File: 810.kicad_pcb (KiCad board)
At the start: 2 copper layers, 148 x 110 mm, 331 parts, among them J1 PJ301BM, J10 PJ301BM, J11 PJ301BM, J12 PJ301BM, J13 PJ301BM, J14 PJ301BM, J15 JACK_MONO_SW, J16 PJ301BM, J17 PJ301B, J18 PJ301B, J2 PJ301BM, J3 PJ301BM, J4 PJ301B, J5 PJ301B, J6 PJ301BM, J7 PJ301BM, J8 PJ301BM, J9 PJ301BM, P1 CONN_01X08, P2 CONN_02X05, P3 CONN_01X03, P4 CONN_01X08, P5 CONN_01X02, P6 CONN_02X03, Q1 PMBT2369, Q10 2SK208-GR, Q11 2SC4738, Q12 2SA1832, Q13 2SA1832, Q14 2SA1832, Q15 2SC4738, Q2 2SK208-GR, Q3 2SA1618, Q4 2SC4207, Q5 2SK208-GR, Q6 MMBF4391LT1G, Q7 2SA1832, Q8 PMBT2369, Q9 2SK208-GR, SW1 SPDT, SW2 SPDT, SW3 BF3-1050, SW4 SPDT, SW5 DP6T-ALPHA-SR2511, U1 TL072-, U10 TL072-, U11 TL072-, U12 TA75S558F, U13 TA75S558F, U14 TA75S558F, U15 TA75S558F, U16 TA75S558F, U17 CD4052, U18 TA75S558F, U19 TL072-, U2 TL072-, U20 CD4013, U3 TL072-, U4 CD40106, U5 CD4027, U6 LM13700, U7 LM13700, U8 LM13700, U9 TL072-

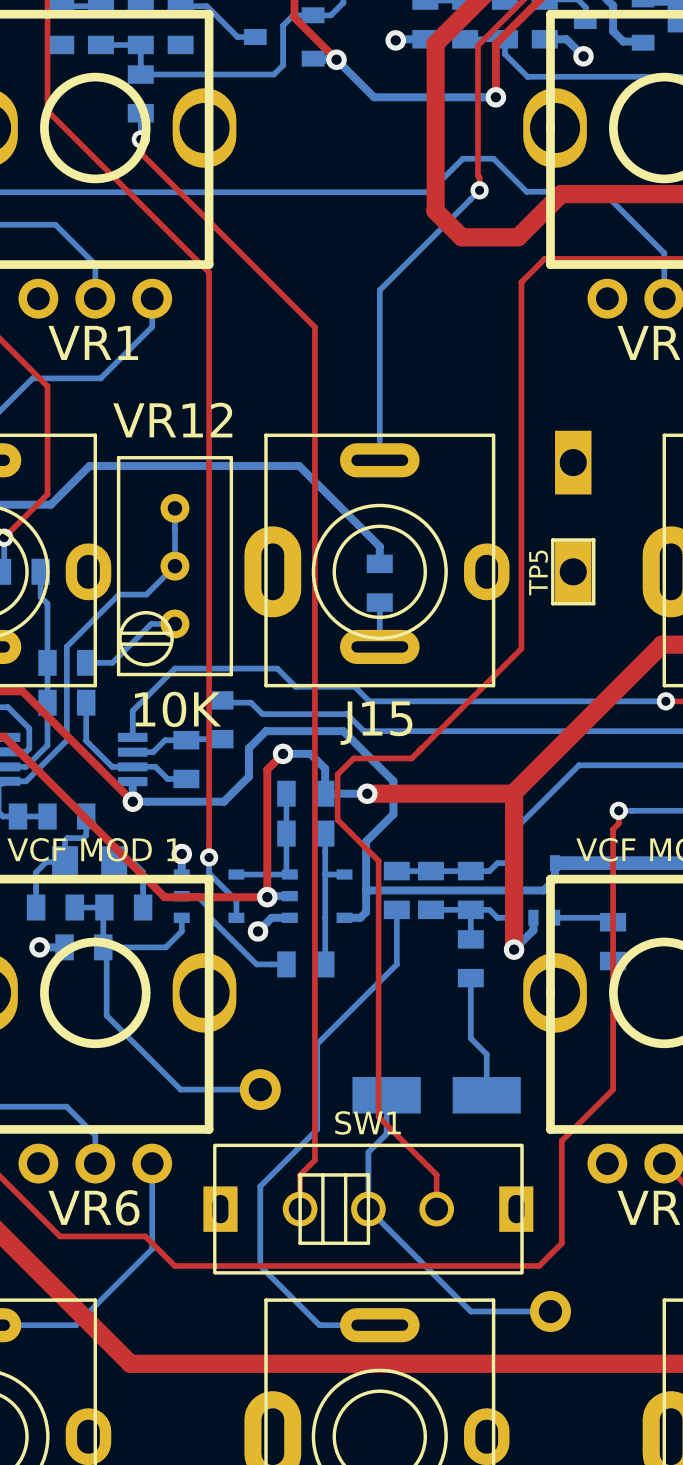
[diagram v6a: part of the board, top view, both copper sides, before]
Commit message: fixed position of middle switch, offset by 0.5 mm
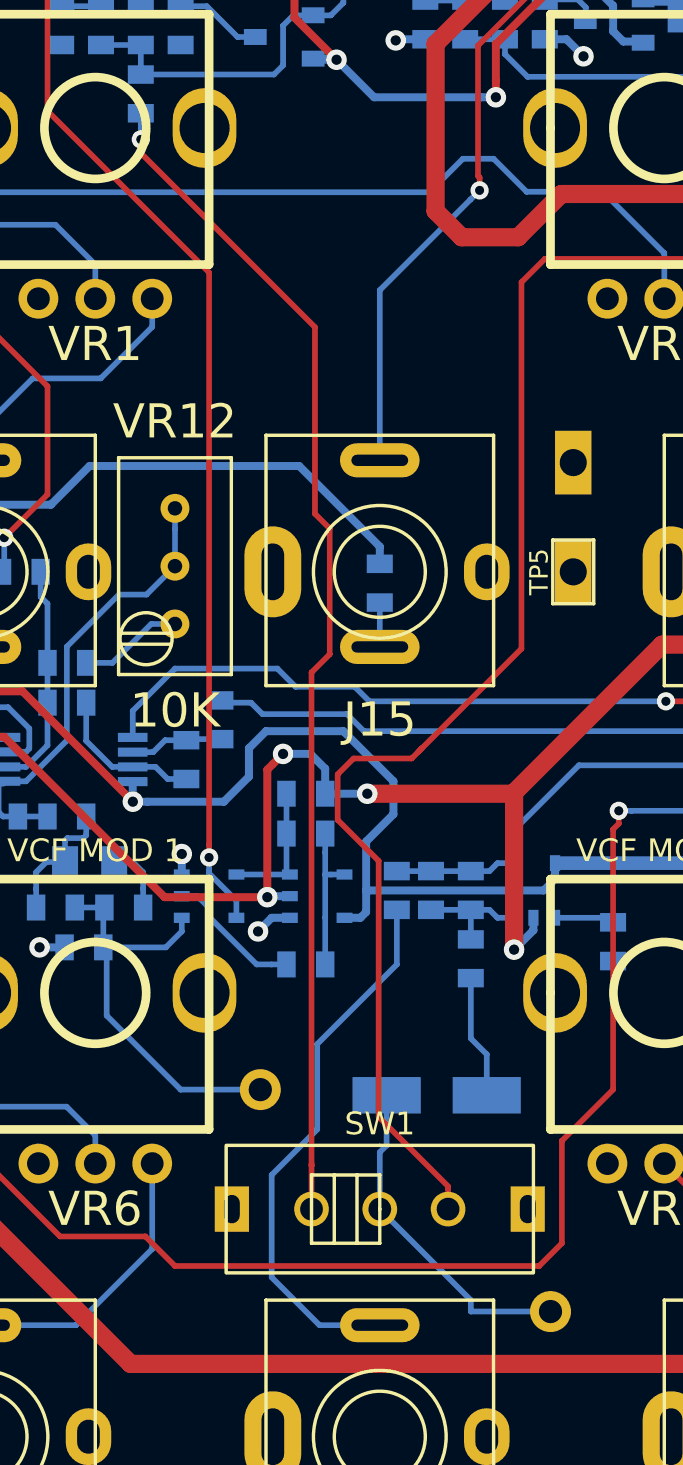
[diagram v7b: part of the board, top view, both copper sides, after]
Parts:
- moved SW1 0.50 mm to (158.0, 135.5)
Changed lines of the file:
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@@
     (area 78.467857 38.411038 232.878334 151.100001)
     (thickness 1.6)
-    (drawings 152)
-    (tracks 2178)
+    (drawings 148)
+    (tracks 2183)
     (zones 0)
     (modules 331)
@@
     (34 B.Paste user)
     (35 F.Paste user)
-    (36 B.SilkS user)
+    (36 B.SilkS user hide)
     (37 F.SilkS user)
     (38 B.Mask user)
@@
     (40 Dwgs.User user)
     (41 Cmts.User user)
-    (42 Eco1.User user hide)
+    (42 Eco1.User user)
     (43 Eco2.User user)
     (44 Edge.Cuts user)
@@
     (pad_to_paste_clearance -0.05)
     (aux_axis_origin 0 0)
-    (visible_elements 7FFFF7FF)
+    (visible_elements 7FFCF7FF)
     (pcbplotparams
-      (layerselection 0x010f0_80000001)
-      (usegerberextensions true)
-      (excludeedgelayer true)
+      (layerselection 0x01400_00000000)
+      (usegerberextensions false)
+      (excludeedgelayer false)
       (linewidth 0.200000)
       (plotframeref false)
@@
       (plotinvisibletext false)
       (padsonsilk false)
-      (subtractmaskfromsilk true)
-      (outputformat 1)
+      (subtractmaskfromsilk false)
+      (outputformat 3)
       (mirror false)
       (drillshape 0)
@@
   )
   (module MyModules:SS-12F108-1P2T-SLIDE (layer F.Cu)
-    (at 157.5 135.5)
+    (at 158 135.5)
     (descr http://www.taydaelectronics.com/datasheets/A-5111.pdf)
     (tags "1P2T, A-5111, TAYDA")
@@
   (gr_line (start 96.74 99.97) (end 94.46 99.97) (angle 90) (layer Eco1.User) (width 0.2))
   (gr_line (start 95.5 98.75) (end 95.5 101) (angle 90) (layer Eco1.User) (width 0.2))
-  (gr_line (start 209.5 132) (end 206.5 132) (angle 90) (layer Eco1.User) (width 0.2))
-  (gr_line (start 208 130.5) (end 208 133.75) (angle 90) (layer Eco1.User) (width 0.2))
-  (gr_line (start 159.5 132) (end 156.5 132) (angle 90) (layer Eco1.User) (width 0.2))
-  (gr_line (start 158 130.5) (end 158 133.5) (angle 90) (layer Eco1.User) (width 0.2))
-  (gr_line (start 109.5 132) (end 106.5 132) (angle 90) (layer Eco1.User) (width 0.2))
-  (gr_line (start 108 130.5) (end 108 133.5) (angle 90) (layer Eco1.User) (width 0.2))
+  (gr_line (start 209.5 135.5) (end 206.5 135.5) (angle 90) (layer Eco1.User) (width 0.2))
+  (gr_line (start 208 134) (end 208 137.25) (angle 90) (layer Eco1.User) (width 0.2))
+  (gr_line (start 159.5 135.5) (end 156.5 135.5) (angle 90) (layer Eco1.User) (width 0.2))
+  (gr_line (start 158 134) (end 158 137) (angle 90) (layer Eco1.User) (width 0.2))
+  (gr_line (start 109.5 135.5) (end 106.5 135.5) (angle 90) (layer Eco1.User) (width 0.2))
+  (gr_line (start 108 134) (end 108 137) (angle 90) (layer Eco1.User) (width 0.2))
   (gr_line (start 146.63 110.44) (end 148.88 110.44) (layer Eco1.User) (width 0.1))
   (gr_line (start 147.73 109.29) (end 147.73 111.6) (layer Eco1.User) (width 0.1))
@@
   (gr_line (start 158.001092 147.500117) (end 158.001092 143.500117) (layer Eco1.User) (width 0.1))
   (gr_line (start 156.00109 145.500117) (end 160.00109 145.500117) (layer Eco1.User) (width 0.1))
-  (gr_line (start 158.001092 139.428279) (end 158.001092 135.428279) (layer Eco1.User) (width 0.1))
-  (gr_line (start 156.00109 137.428279) (end 160.00109 137.428279) (layer Eco1.User) (width 0.1))
   (gr_line (start 175.501093 147.500117) (end 175.501093 143.500117) (layer Eco1.User) (width 0.1))
   (gr_line (start 173.501092 145.500117) (end 177.501092 145.500117) (layer Eco1.User) (width 0.1))
@@
   (gr_line (start 208.001099 147.500117) (end 208.001099 143.500117) (layer Eco1.User) (width 0.1))
   (gr_line (start 206.001097 145.500117) (end 210.001098 145.500117) (layer Eco1.User) (width 0.1))
-  (gr_line (start 208.001099 139.428279) (end 208.001099 135.428279) (layer Eco1.User) (width 0.1))
-  (gr_line (start 206.001097 137.428279) (end 210.001098 137.428279) (layer Eco1.User) (width 0.1))
   (gr_line (start 220.501088 128.004471) (end 220.501088 124.004471) (layer Eco1.User) (width 0.1))
   (gr_line (start 218.501086 126.004471) (end 222.501087 126.004471) (layer Eco1.User) (width 0.1))
@@
   (segment (start 175.80086 83.25) (end 175.55086 83) (width 0.25) (layer B.Cu) (net 33))
   (segment (start 159.85 115.25) (end 159.4 115.7) (width 0.25) (layer F.Cu) (net 34))
-  (segment (start 156.85 115.7) (end 156.15 116.4) (width 0.25) (layer F.Cu) (net 34))
-  (segment (start 156.15 116.4) (end 156.15 118.4) (width 0.25) (layer F.Cu) (net 34))
   (segment (start 157.95001 120.20001) (end 157.95001 131.45001) (width 0.25) (layer F.Cu) (net 34))
   (segment (start 159.4 115.7) (end 156.85 115.7) (width 0.25) (layer F.Cu) (net 34))
+  (segment (start 156.85 115.7) (end 156.15 116.4) (width 0.25) (layer F.Cu) (net 34))
+  (segment (start 156.15 116.4) (end 156.15 118.4) (width 0.25) (layer F.Cu) (net 34))
+  (segment (start 161 134.5) (end 161 134.6) (width 0.25) (layer F.Cu) (net 34))
   (segment (start 156.15 118.4) (end 157.95001 120.20001) (width 0.25) (layer F.Cu) (net 34))
-  (segment (start 157.95001 131.45001) (end 160.5 134) (width 0.25) (layer F.Cu) (net 34))
-  (segment (start 160.5 134) (end 160.5 135.5) (width 0.25) (layer F.Cu) (net 34))
+  (segment (start 157.95001 131.45001) (end 161 134.5) (width 0.25) (layer F.Cu) (net 34))
+  (segment (start 161 134.6) (end 161 135.5) (width 0.25) (layer F.Cu) (net 34))
   (segment (start 159.85 115.25) (end 164.22498 110.87502) (width 0.25) (layer F.Cu) (net 34))
   (segment (start 164.22498 110.87502) (end 164.22498 94.77502) (width 0.25) (layer F.Cu) (net 34))
@@
   (segment (start 162 125.3509) (end 162 128) (width 0.25) (layer B.Cu) (net 36))
   (segment (start 163.25 130.30036) (end 163 130.55036) (width 0.25) (layer B.Cu) (net 36))
-  (segment (start 158.30036 130.5) (end 158.30036 132.19964) (width 0.25) (layer B.Cu) (net 37))
-  (segment (start 158.30036 132.19964) (end 157.5 133) (width 0.25) (layer B.Cu) (net 37))
-  (segment (start 157.5 133) (end 157.5 135.5) (width 0.25) (layer B.Cu) (net 37))
-  (segment (start 157.5 135.5) (end 162 140) (width 0.25) (layer B.Cu) (net 37))
+  (segment (start 158.30036 130.5) (end 158.30036 132.69964) (width 0.25) (layer B.Cu) (net 37))
+  (segment (start 158.30036 132.69964) (end 158 133) (width 0.25) (layer B.Cu) (net 37))
+  (segment (start 158 133) (end 158 135.5) (width 0.25) (layer B.Cu) (net 37))
+  (segment (start 162 140) (end 162 139.5) (width 0.25) (layer B.Cu) (net 37))
+  (segment (start 162 139.5) (end 158 135.5) (width 0.25) (layer B.Cu) (net 37))
   (segment (start 162 140) (end 165.5 140) (width 0.25) (layer B.Cu) (net 37))
   (segment (start 162 122.3509) (end 162 123.6491) (width 0.25) (layer B.Cu) (net 38))
@@
   (segment (start 110.7991 140.6) (end 110.8991 140.5) (width 0.25) (layer B.Cu) (net 89))
   (segment (start 158.75 122.3509) (end 158.75 124.75) (width 0.25) (layer B.Cu) (net 91))
+  (segment (start 153.25 138.5) (end 155.35 140.6) (width 0.25) (layer B.Cu) (net 91))
   (segment (start 158.75 124.75) (end 155.25 128.25) (width 0.25) (layer B.Cu) (net 91))
+  (segment (start 155.25 132) (end 153.25 134) (width 0.25) (layer B.Cu) (net 91))
   (segment (start 155.25 128.25) (end 155.25 132) (width 0.25) (layer B.Cu) (net 91))
-  (segment (start 155.25 132) (end 152.75 134.5) (width 0.25) (layer B.Cu) (net 91))
-  (segment (start 152.75 134.5) (end 152.75 138) (width 0.25) (layer B.Cu) (net 91))
-  (segment (start 152.75 138) (end 155.35 140.6) (width 0.25) (layer B.Cu) (net 91))
+  (segment (start 153.25 134) (end 153.25 138.5) (width 0.25) (layer B.Cu) (net 91))
   (segment (start 155.35 140.6) (end 158 140.6) (width 0.25) (layer B.Cu) (net 91))
   (segment (start 196.74 89.33) (end 197.5 90.09) (width 0.25) (layer F.Cu) (net 93))
@@
   (segment (start 183.75 68.3991) (end 183.75 67) (width 0.25) (layer B.Cu) (net 164))
   (via (at 183.75 67) (size 0.8) (drill 0.4) (layers F.Cu B.Cu) (net 164))
-  (segment (start 154.5 135.5) (end 154.5 134) (width 0.25) (layer F.Cu) (net 165))
-  (segment (start 154.5 134) (end 155.15 133.35) (width 0.25) (layer F.Cu) (net 165))
-  (segment (start 155.15 96.75) (end 147.5 89.1) (width 0.25) (layer F.Cu) (net 165))
-  (segment (start 155.15 133.35) (end 155.15 96.75) (width 0.25) (layer F.Cu) (net 165))
-  (segment (start 147.5 88.5) (end 147.5 88.500002) (width 0.25) (layer F.Cu) (net 165))
-  (segment (start 147.5 89.1) (end 147.5 88.5) (width 0.25) (layer F.Cu) (net 165))
+  (segment (start 155 133.6) (end 155 135.5) (width 0.25) (layer F.Cu) (net 165))
+  (segment (start 155 133.6) (end 155 133.5) (width 0.25) (layer F.Cu) (net 165))
+  (segment (start 147.5 88.500002) (end 147.5 89.1) (width 0.25) (layer F.Cu) (net 165))
+  (segment (start 147.5 89.1) (end 155.15 96.75) (width 0.25) (layer F.Cu) (net 165))
+  (segment (start 155.15 96.75) (end 155.15 104.95) (width 0.25) (layer F.Cu) (net 165))
+  (segment (start 155 111.920293) (end 155 133.6) (width 0.25) (layer F.Cu) (net 165))
+  (segment (start 155.15 104.95) (end 155.8 105.6) (width 0.25) (layer F.Cu) (net 165))
+  (segment (start 155.8 105.6) (end 155.8 111.120293) (width 0.25) (layer F.Cu) (net 165))
+  (segment (start 155.8 111.120293) (end 155 111.920293) (width 0.25) (layer F.Cu) (net 165))
   (via (at 147.5 88.500002) (size 0.8) (drill 0.4) (layers F.Cu B.Cu) (net 165))
   (segment (start 147.5 87.3509) (end 147.5 88.500002) (width 0.25) (layer B.Cu) (net 165))

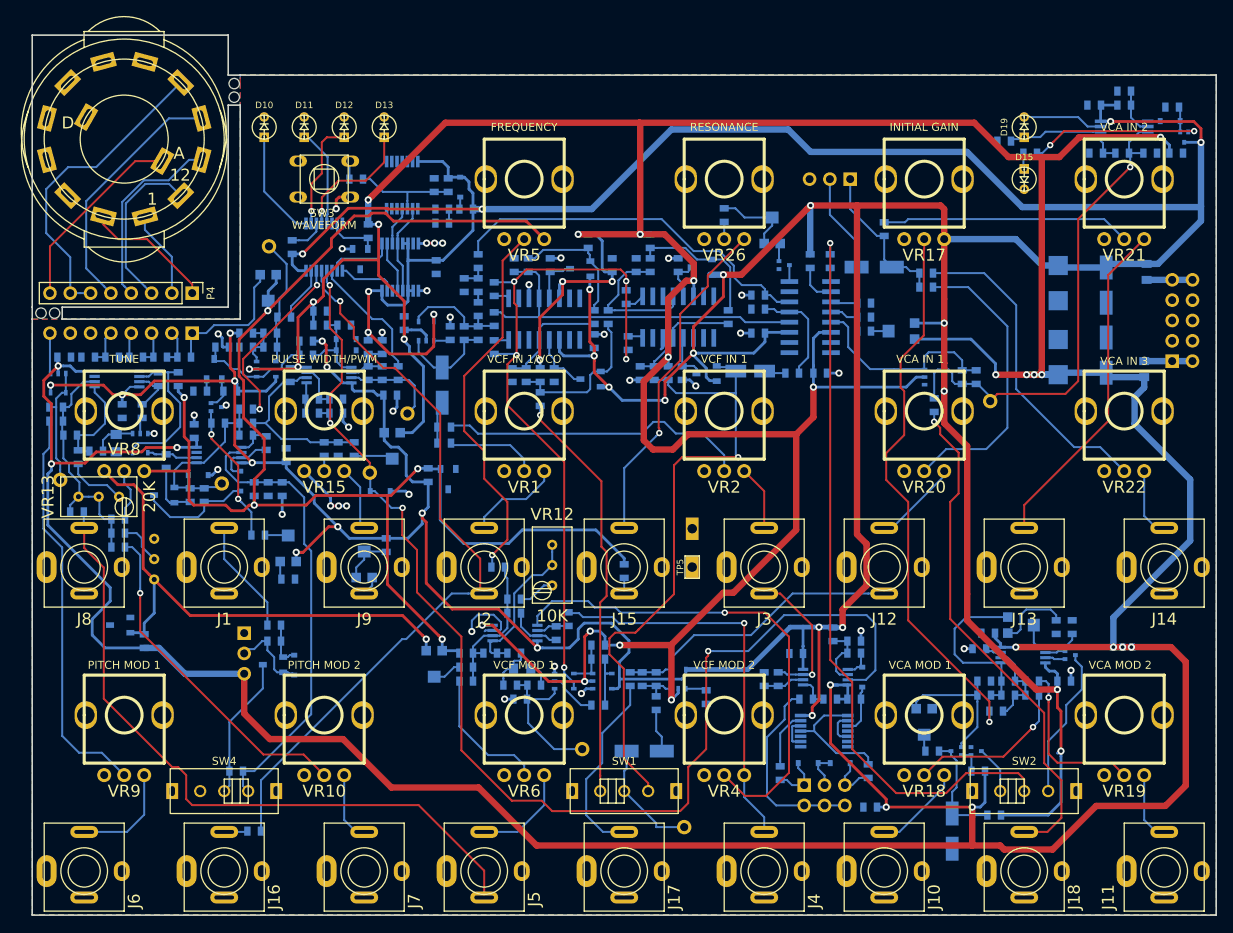
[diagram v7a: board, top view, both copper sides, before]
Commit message: ground plane stiching and tweaking
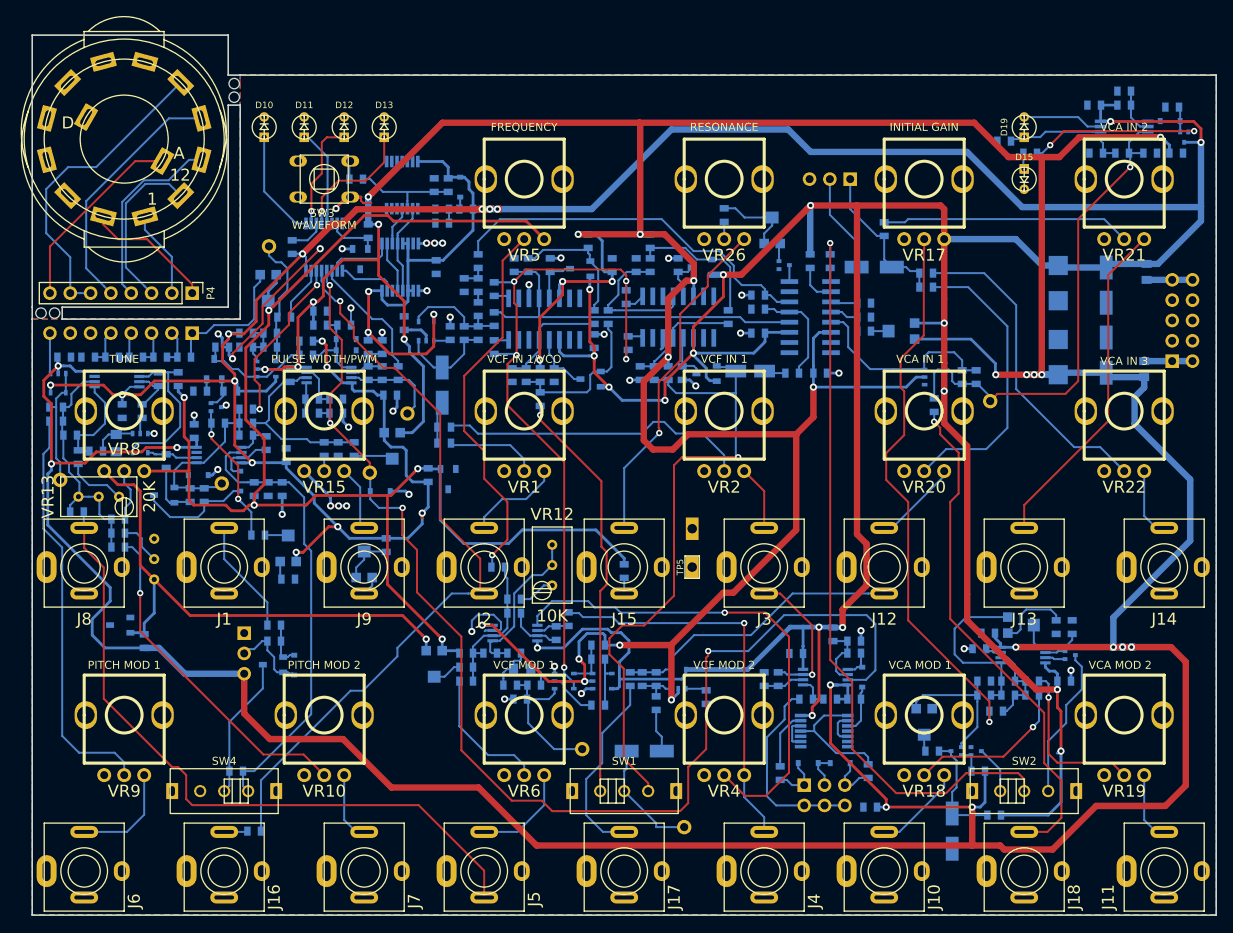
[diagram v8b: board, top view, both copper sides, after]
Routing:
- net GND: track 64.6 -> 90.7 mm, vias 36 -> 39
- net +12V: track 742.9 -> 730.9 mm, vias 32 -> 34
- net +10V: track 188.1 -> 186.4 mm
- net VCO_SAW: track 22.9 -> 21.7 mm
- net -12V: track 814.9 -> 813.8 mm
- net Net-(R30-Pad1): track 50.4 -> 51.4 mm
- net VCO: track 93.8 -> 94.5 mm
- net VCO_PULSE: track 156.8 -> 157.4 mm
- added copper zone on F.Cu, net +12V
